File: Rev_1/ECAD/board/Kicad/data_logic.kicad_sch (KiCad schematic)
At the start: 87 parts, among them SW300 6x6, SW301 6x6, SW302 6x6, SW303 6x6, U301 74HC245, U302 74HC245, U303 74HC595, U304 74HC595, U305 74HC595, U306 AT28C64B-15PU, U307 Summer

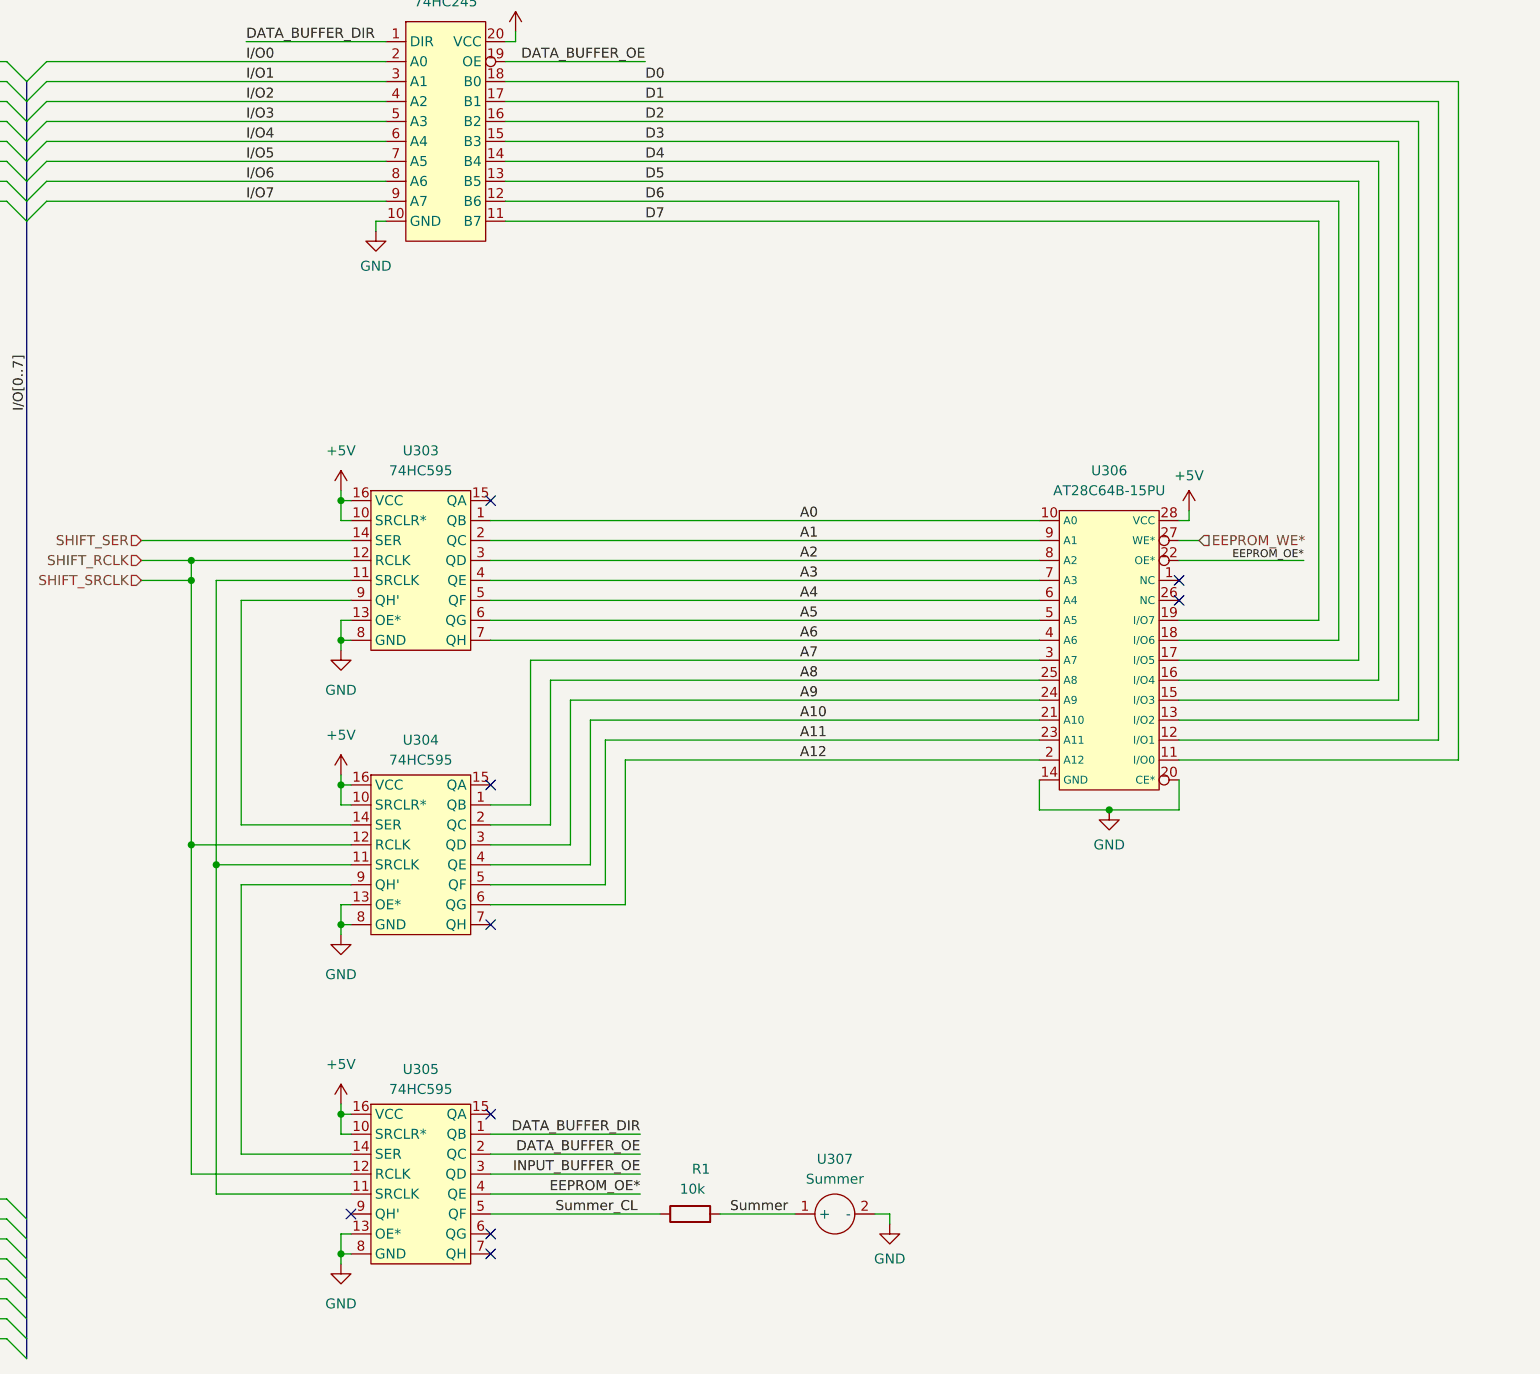
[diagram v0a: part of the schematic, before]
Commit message: Made changes to the wiring in the shcematic to make it easier to route on the pcb, U305
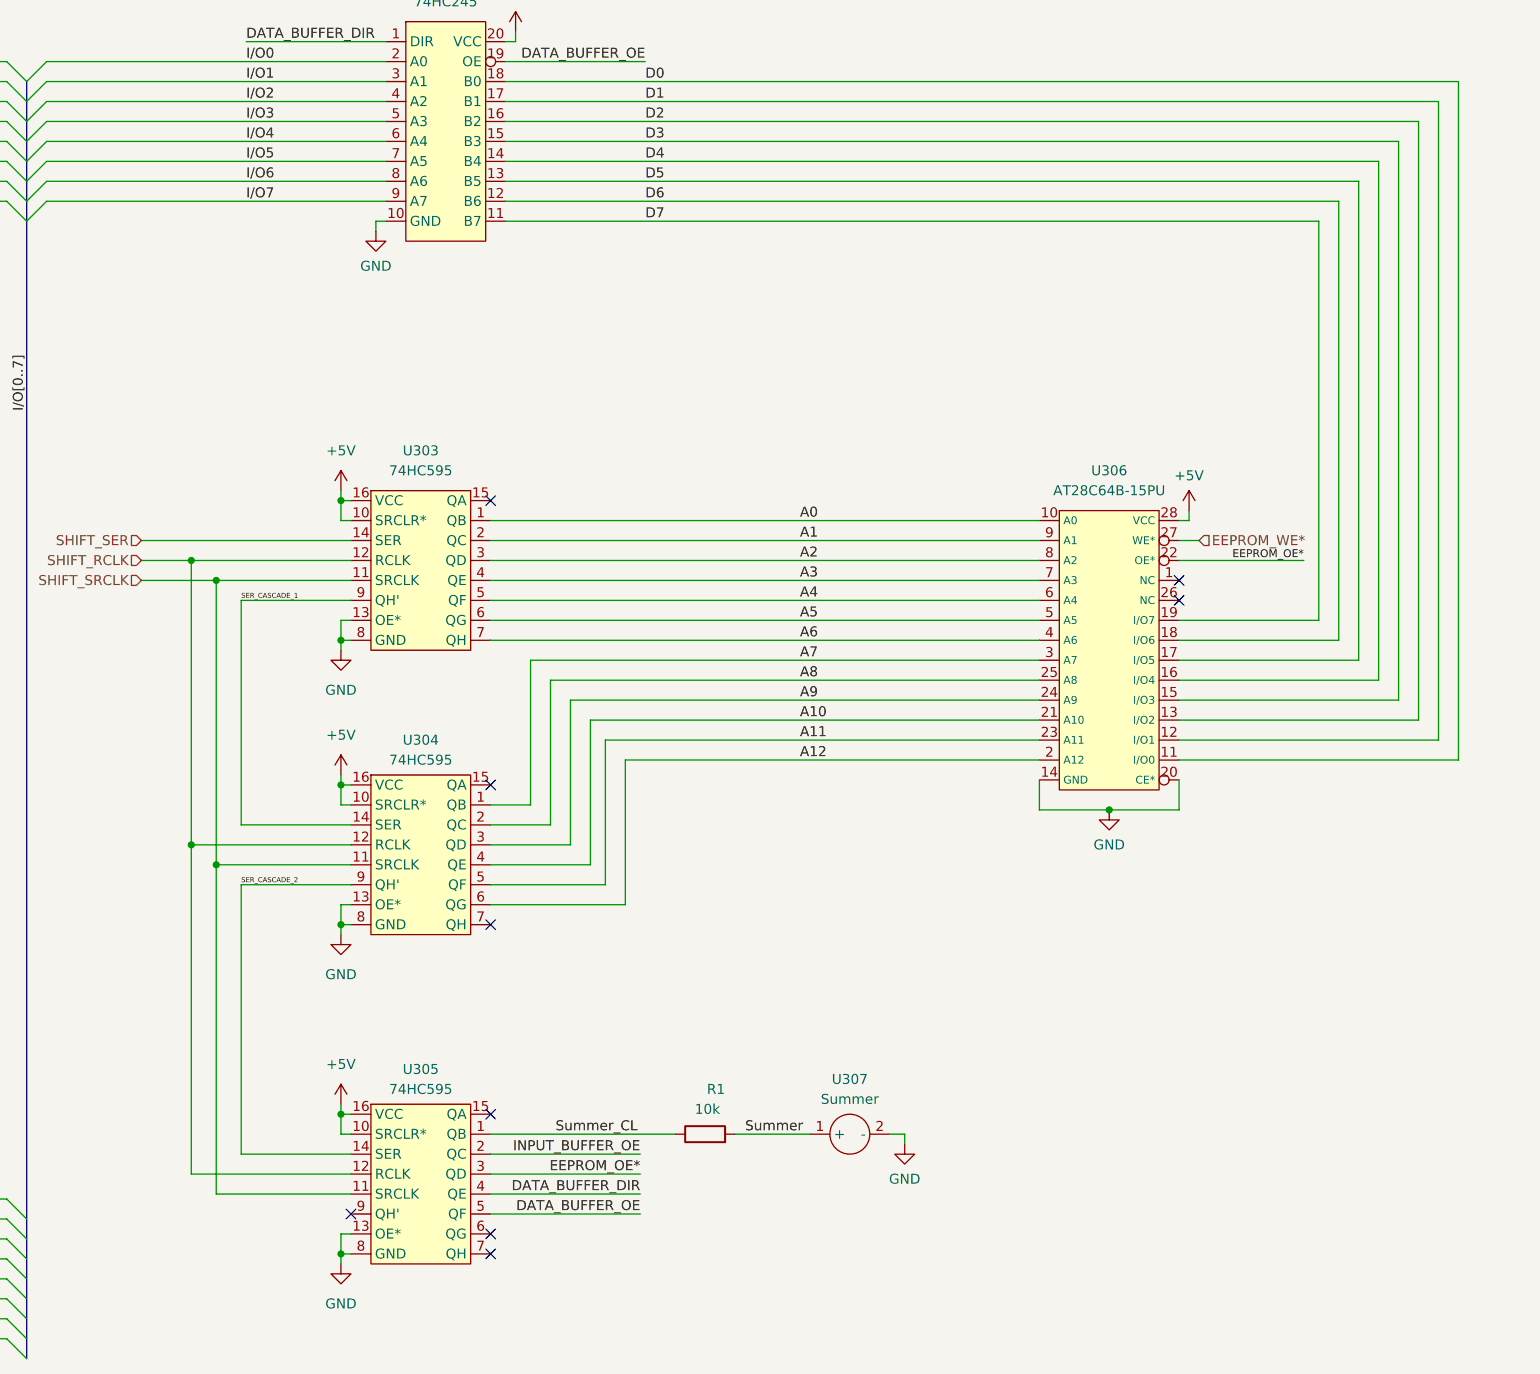
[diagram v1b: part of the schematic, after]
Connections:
- net DATA_BUFFER_DIR: now also U305.4 (QE); no longer U305.1 (QB)
- net DATA_BUFFER_OE: now also U305.5 (QF); no longer U305.2 (QC)
- net EEPROM_OE*: now also U305.3 (QD); no longer U305.4 (QE)
- net INPUT_BUFFER_OE: now also U305.2 (QC); no longer U305.3 (QD)
- net Summer_CL: now also U305.1 (QB); no longer U305.5 (QF)
- net SHIFT_SRCLK: now reaches U303.11 (SRCLK), U304.11 (SRCLK), U305.11 (SRCLK)
- net SER_CASCADE_1: now reaches U303.9 (QH'), U304.14 (SER)
- net SER_CASCADE_2: now reaches U304.9 (QH'), U305.14 (SER)
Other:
- moved on the sheet: R1, U307

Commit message: Made some progress on the pcb
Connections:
- net BUTTON_1: now also U301.13 (B5); no longer U301.18 (B0)
- net BUTTON_2: now also U301.14 (B4); no longer U301.17 (B1)
- net BUTTON_3: now also U301.15 (B3); no longer U301.16 (B2)
- net BUTTON_4: now also U301.16 (B2); no longer U301.15 (B3)
- net ROT_A: no longer C101.2, R1.2, U301.13 (B5)
- net ROT_B: no longer C101.2, R1.2, U301.14 (B4)
- new net ROT_A_INPT: C101.2, R1.2, U301.17 (B1)
- new net ROT_B_INPT: C101.2, R1.2, U301.18 (B0)
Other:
- moved on the sheet: C101, R1, U300
